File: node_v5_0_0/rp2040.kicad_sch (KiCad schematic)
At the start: 32 parts, among them SW1 PTS636 SM50J SMTR LFS, SW2 PTS636 SM50J SMTR LFS, SW3 PTS636 SM50J SMTR LFS, U1 RP2040, U14 W25Q128, U2 USBLC6-2SC6

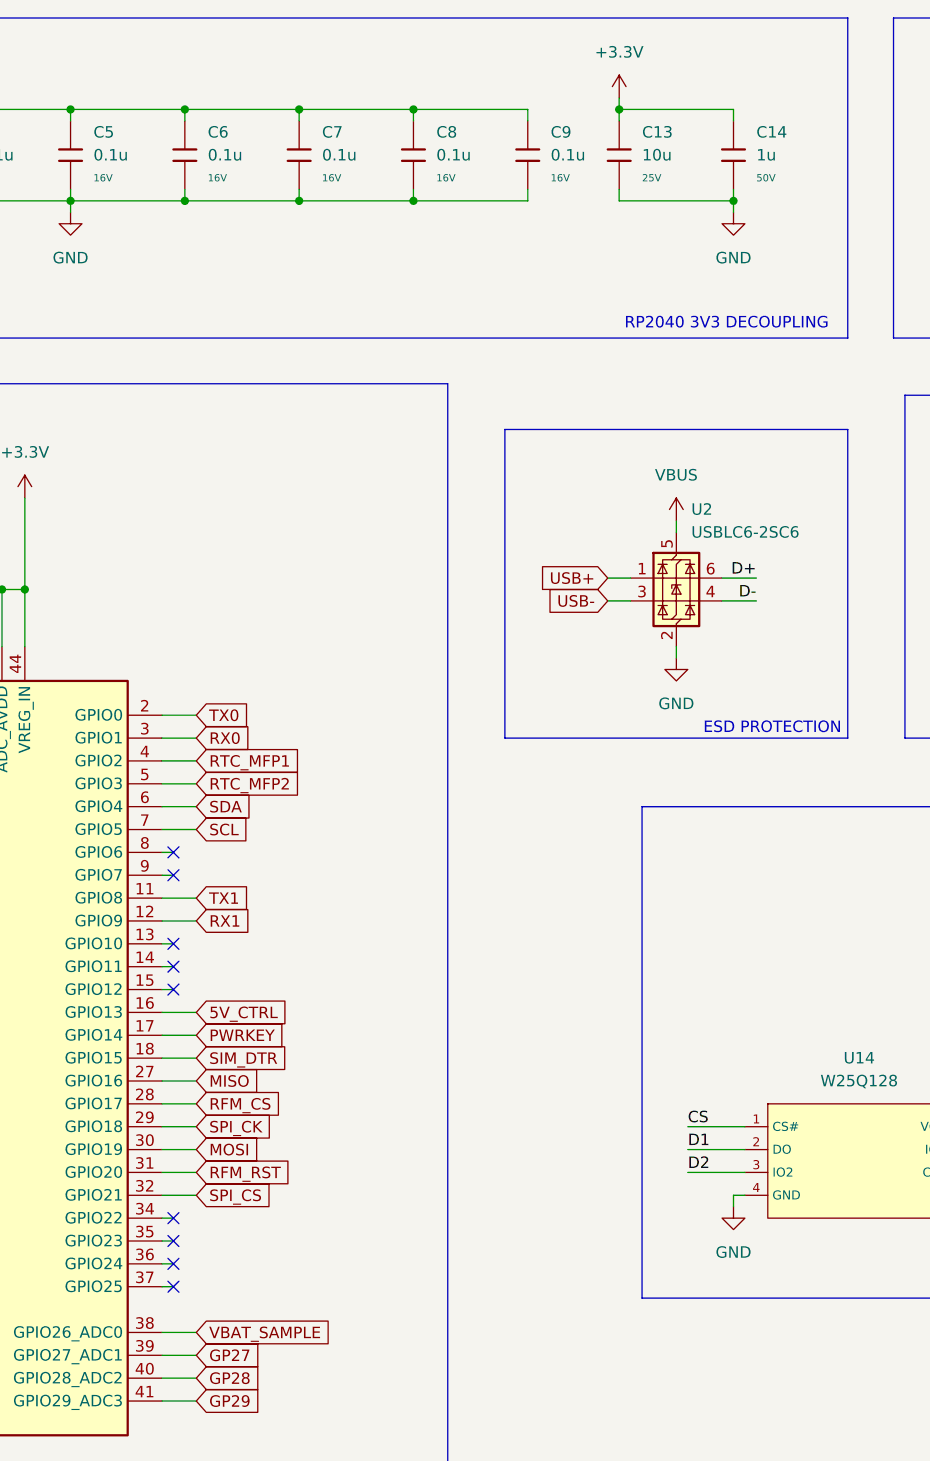
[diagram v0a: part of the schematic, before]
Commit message: updated layout
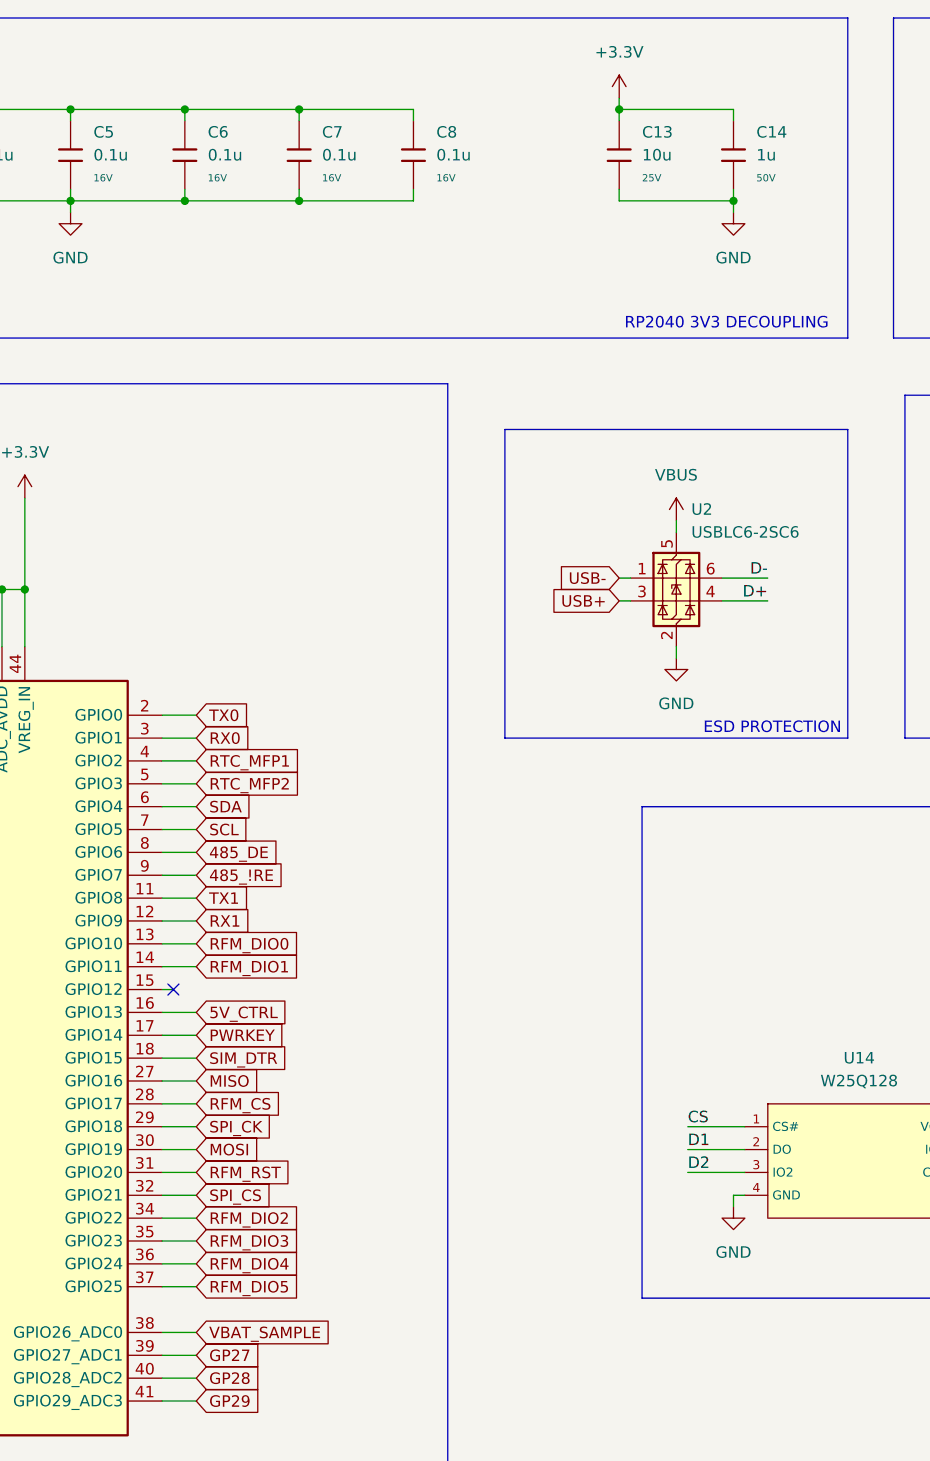
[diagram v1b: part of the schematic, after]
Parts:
- removed C9: 0.1u, JLCPCB-Kicad-Footprints:C_0402, symbol JLCPCB-Capacitors:0402,100nF
- SW1, SW2, SW3: footprint SW_PTS636_CNK -> WiSDOM:SW_PTS636_CNK
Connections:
- net D+: now also U2.4 (I/O2); no longer U2.6 (I/O1)
- net D-: now also U2.6 (I/O1); no longer U2.4 (I/O2)
- net USB+: now also U2.3 (I/O2); no longer U2.1 (I/O1)
- net USB-: now also U2.1 (I/O1); no longer U2.3 (I/O2)
- net RFM_DIO0: now reaches U1.13 (GPIO10)
- net RFM_DIO1: now reaches U1.14 (GPIO11)
- net RFM_DIO2: now reaches U1.34 (GPIO22)
- net RFM_DIO3: now reaches U1.35 (GPIO23)
- net RFM_DIO4: now reaches U1.36 (GPIO24)
- net RFM_DIO5: now reaches U1.37 (GPIO25)
- net 485_DE: now reaches U1.8 (GPIO6)
- net 485_!RE: now reaches U1.9 (GPIO7)
- no-connect marks 9 -> 1
